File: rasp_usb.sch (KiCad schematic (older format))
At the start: 20 parts, among them J1 USB_B_Micro, J2 Conn_02x05_Odd_Even, U1 AMS1117-5.0, U2 FT230XQ

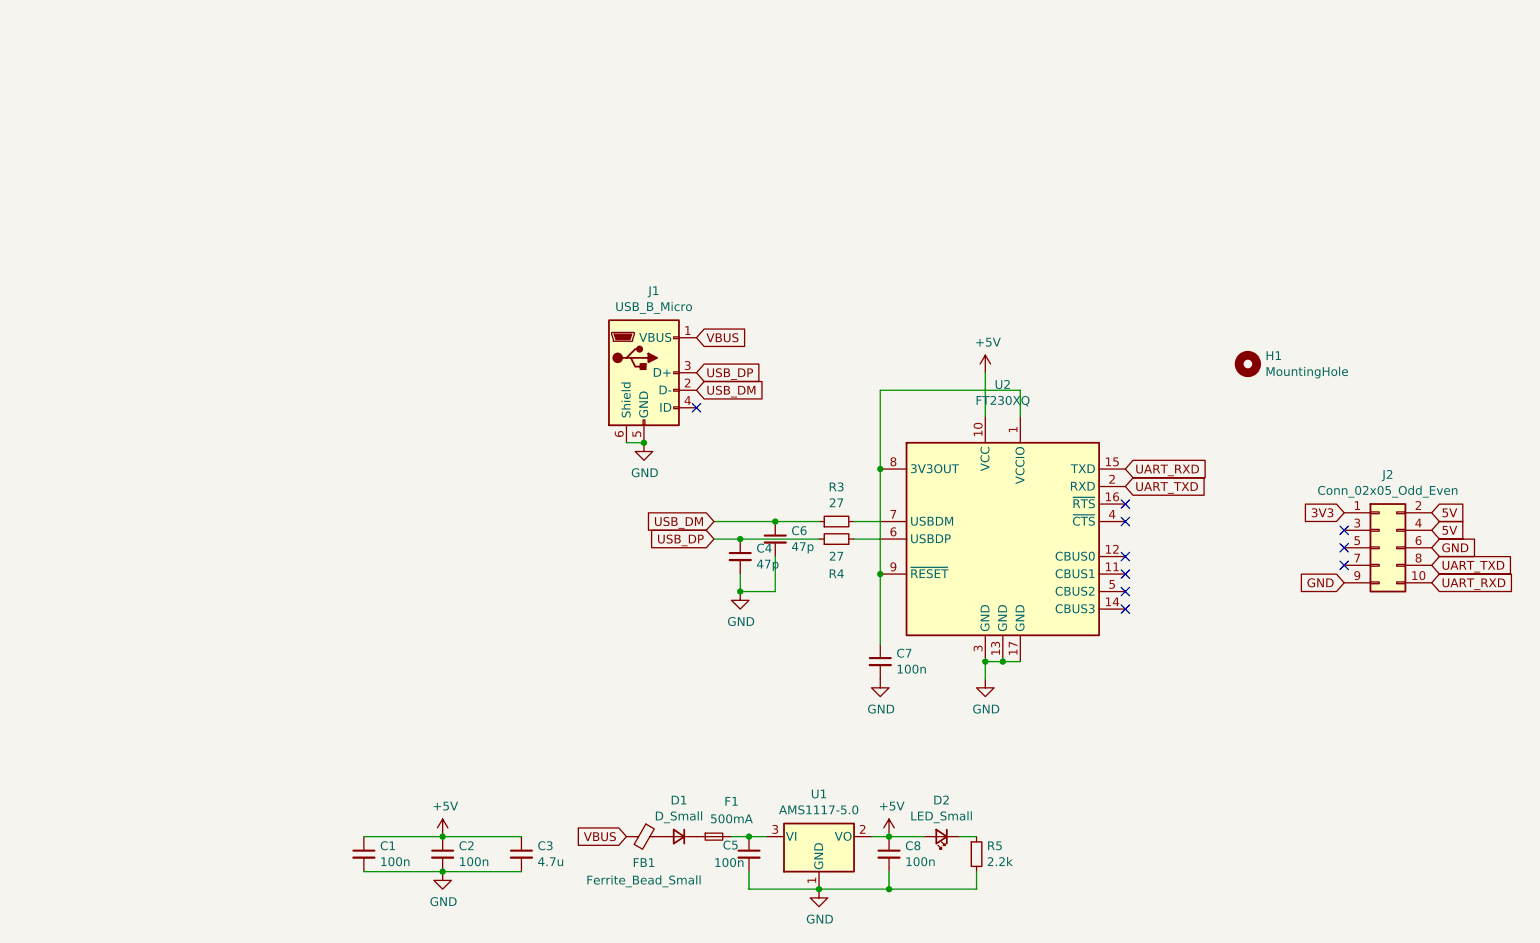
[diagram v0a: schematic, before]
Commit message: ftdi ic is out of stock
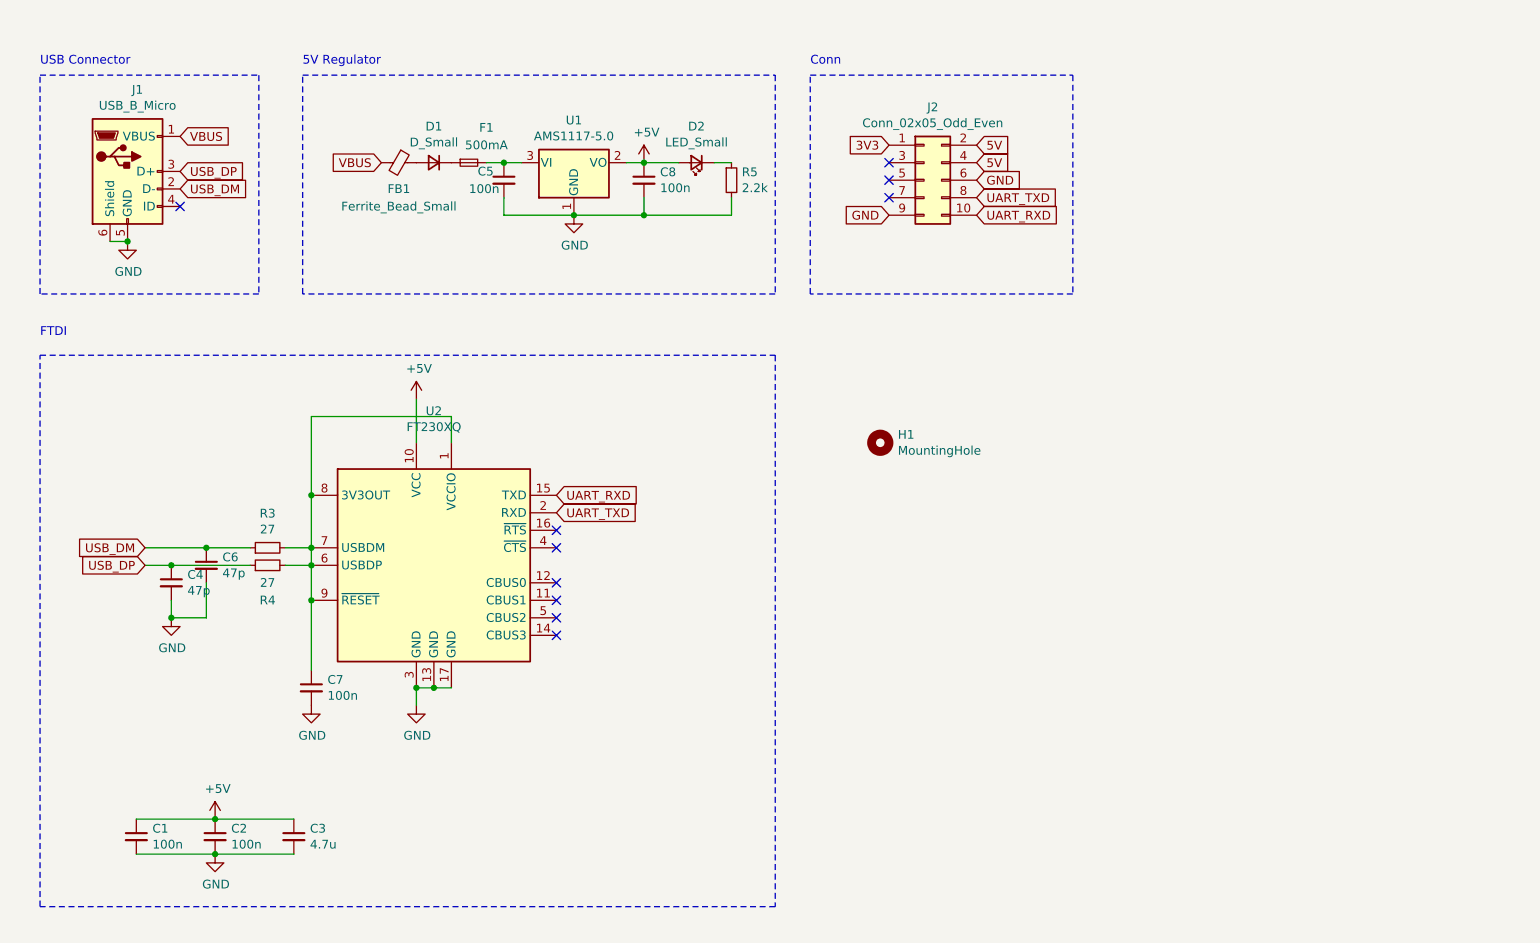
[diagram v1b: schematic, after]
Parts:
- D1: footprint Diode_SMD:D_0603_1608Metric -> Diode_SMD:D_SOD-123
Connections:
- net at C7.1, U2.1 (VCCIO), U2.8 (3V3OUT)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: now also R3.2, R4.2, U2.6 (USBDP), U2.7 (USBDM)
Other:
- note added: "5V Regulator"
- note added: "Conn"
- note added: "FTDI"
- note added: "USB Connector"
- moved on the sheet: C1, C2, C3, C4, C5, C6, C7, C8, D1, D2, F1, FB1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

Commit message: ready to order
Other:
- note added: "USB IC"
- note removed: "FTDI"
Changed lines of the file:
@@
 Wire Notes Line
 	1000 5850 1000 2700
-Text Notes 1000 2600 0    50   ~ 0
-FTDI
 Wire Notes Line
 	1000 1100 2250 1100
@@
 Text Notes 5400 1050 0    50   ~ 0
 Conn
+Text Notes 1050 2650 0    50   ~ 0
+USB IC
 $EndSCHEMATC

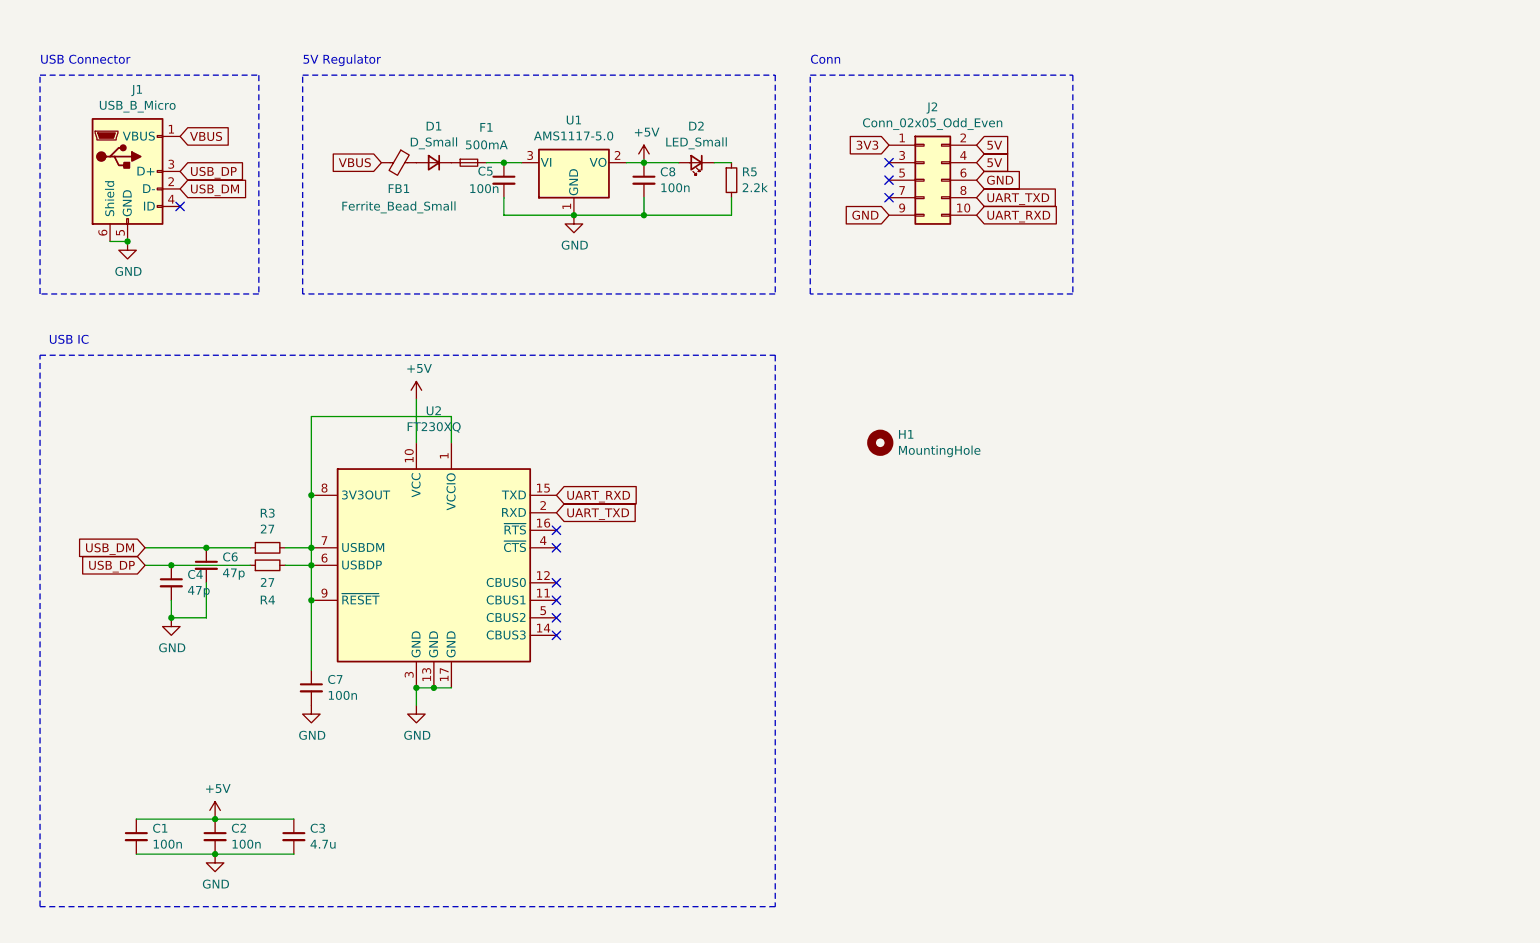
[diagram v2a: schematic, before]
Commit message: Replaced usb IC with cp2104. Ready to order
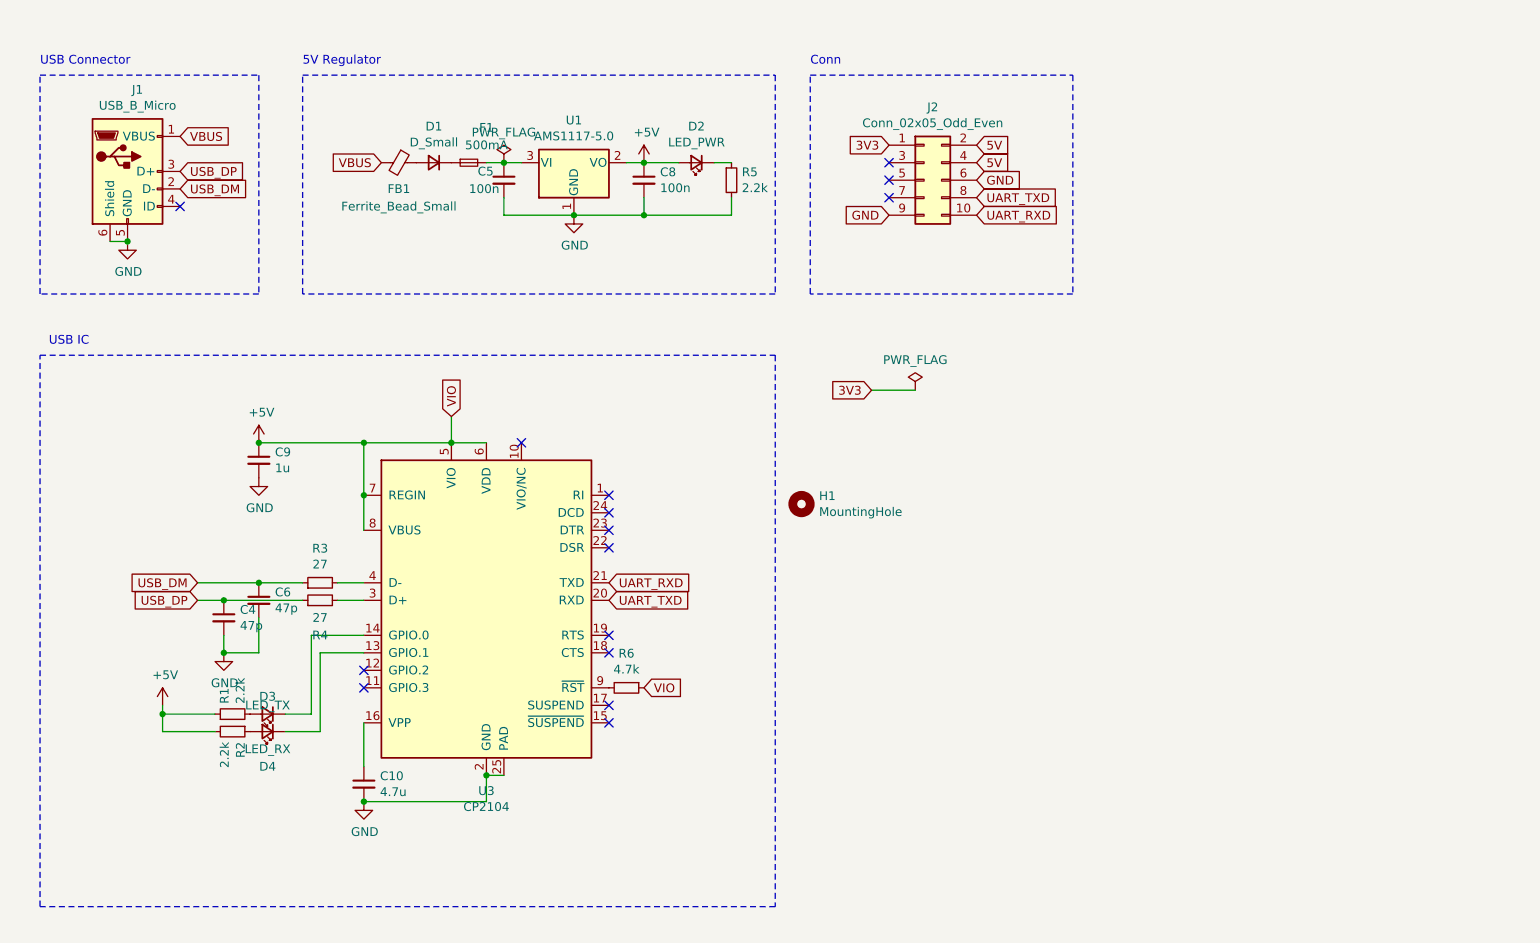
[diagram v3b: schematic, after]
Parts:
- removed C1, C2: 100n, Capacitor_SMD:C_0603_1608Metric, symbol Device:C_Small
- removed C3: 4.7u, Capacitor_SMD:C_0603_1608Metric, symbol Device:C_Small
- removed C7: 100n, Capacitor_SMD:C_0402_1005Metric, symbol Device:C_Small
- removed U2: FT230XQ, Package_DFN_QFN:QFN-16-1EP_4x4mm_P0.65mm_EP2.1x2.1mm, symbol Interface_USB:FT230XQ
- added C10: 4.7u, Capacitor_SMD:C_0603_1608Metric, symbol Device:C_Small
- added C9: 1u, Capacitor_SMD:C_0603_1608Metric, symbol Device:C_Small
- added D3: LED_TX, LED_SMD:LED_0402_1005Metric, symbol Device:LED_Small
- added D4: LED_RX, LED_SMD:LED_0402_1005Metric, symbol Device:LED_Small
- added R1, R2: 2.2k, Resistor_SMD:R_0402_1005Metric, symbol Device:R_Small
- added R6: 4.7k, Resistor_SMD:R_0402_1005Metric, symbol Device:R_Small
- added U3: CP2104, Package_DFN_QFN:QFN-24-1EP_4x4mm_P0.5mm_EP2.6x2.6mm, symbol Interface_USB:CP2104
- D2: value LED_Small -> LED_PWR; footprint LED_SMD:LED_0603_1608Metric -> LED_SMD:LED_0402_1005Metric
- R5: footprint Resistor_SMD:R_0603_1608Metric -> Resistor_SMD:R_0402_1005Metric
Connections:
- net +5V: now also C9.1, R1.1, R2.2, R6.1, U3.5 (VIO), U3.6 (VDD), U3.7 (REGIN), U3.8 (VBUS)
- net GND: now also C10.2, C9.2, U3.2 (GND), U3.25 (PAD)
- net UART_RXD: now also U3.21 (TXD)
- net UART_TXD: now also U3.20 (RXD)
- net at R3.2: now also U3.4 (D-); no longer R4.2
- new net: R4.2, U3.3 (D+)
- new net: D4.1 (K), U3.13 (GPIO.1)
- new net: D3.1 (K), U3.14 (GPIO.0)
- new net: C10.1, U3.16 (VPP)
- new net: R6.2, U3.9 (~RST)
- new net: D3.2 (A), R1.2
- new net: D4.2 (A), R2.1
- no-connect marks 10 -> 15
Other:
- moved on the sheet: C4, C6, H1, R3, R4

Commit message: ready to order
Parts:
- removed H1: MountingHole, MountingHole:MountingHole_2.7mm_M2.5, symbol Mechanical:MountingHole
- J1: footprint Connector_USB:USB_Micro-B_Amphenol_10103594-0001LF_Horizontal -> Connector_USB:USB_Micro-B_Amphenol_10104110_Horizontal
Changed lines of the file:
@@
 Date "2020-11-23"
 Rev ""
-Comp "BitEngineers"
+Comp ""
 Comment1 ""
 Comment2 ""
@@
 Connection ~ 4450 1900
 $Comp
-L Mechanical:MountingHole H1
-U 1 1 5FCD5980
-P 5350 3550
-F 0 "H1" H 5450 3596 50  0000 L CNN
-F 1 "MountingHole" H 5450 3505 50  0000 L CNN
-F 2 "MountingHole:MountingHole_2.7mm_M2.5" H 5350 3550 50  0001 C CNN
-F 3 "~" H 5350 3550 50  0001 C CNN
-	1    5350 3550
-	1    0    0    -1
-$EndComp
-$Comp
 L Connector:USB_B_Micro J1
 U 1 1 5FD1A450
@@
 F 0 "J1" H 1557 2117 50  0000 C CNN
 F 1 "USB_B_Micro" H 1557 2026 50  0000 C CNN
-F 2 "Connector_USB:USB_Micro-B_Amphenol_10103594-0001LF_Horizontal" H 1650 1600 50  0001 C CNN
+F 2 "Connector_USB:USB_Micro-B_Amphenol_10104110_Horizontal" H 1650 1600 50  0001 C CNN
 F 3 "~" H 1650 1600 50  0001 C CNN
 	1    1500 1650

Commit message: Updated schematics as hierarchical structure
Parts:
- removed C10: 4.7u, Capacitor_SMD:C_0603_1608Metric, symbol Device:C_Small
- removed C4, C6: 47p, Capacitor_SMD:C_0402_1005Metric, symbol Device:C_Small
- removed C5, C8: 100n, Capacitor_SMD:C_0603_1608Metric, symbol Device:C_Small
- removed C9: 1u, Capacitor_SMD:C_0603_1608Metric, symbol Device:C_Small
- removed D1: D_Small, Diode_SMD:D_SOD-123, symbol Device:D_Small
- removed D2: LED_PWR, LED_SMD:LED_0402_1005Metric, symbol Device:LED_Small
- removed D3: LED_TX, LED_SMD:LED_0402_1005Metric, symbol Device:LED_Small
- removed D4: LED_RX, LED_SMD:LED_0402_1005Metric, symbol Device:LED_Small
- removed F1: 500mA, Fuse:Fuse_0603_1608Metric, symbol Device:Fuse_Small
- removed FB1: Ferrite_Bead_Small, Inductor_SMD:L_0603_1608Metric, symbol Device:Ferrite_Bead_Small
- removed J1: USB_B_Micro, Connector_USB:USB_Micro-B_Amphenol_10104110_Horizontal, symbol Connector:USB_B_Micro
- removed R1, R2, R5: 2.2k, Resistor_SMD:R_0402_1005Metric, symbol Device:R_Small
- removed R3, R4: 27, Resistor_SMD:R_0402_1005Metric, symbol Device:R_Small
- removed R6: 4.7k, Resistor_SMD:R_0402_1005Metric, symbol Device:R_Small
- removed U1: AMS1117-5.0, Package_TO_SOT_SMD:SOT-223-3_TabPin2, symbol Regulator_Linear:AMS1117-5.0
- removed U3: CP2104, Package_DFN_QFN:QFN-24-1EP_4x4mm_P0.5mm_EP2.6x2.6mm, symbol Interface_USB:CP2104
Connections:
- no-connect marks 15 -> 3
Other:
- note removed: "5V Regulator"
- note removed: "USB Connector"
- note removed: "USB IC"

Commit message: annotation number
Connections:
- net 3V3 renamed +3V3
- net 5V renamed +5V
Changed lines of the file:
@@
 	1    0    0    -1
 $EndComp
-Text GLabel 6350 1500 2    50   Input ~ 0
-5V
-Text GLabel 6350 1700 2    50   Input ~ 0
-GND
 Text GLabel 6350 1800 2    50   Input ~ 0
 UART_TXD
 Text GLabel 6350 1900 2    50   Input ~ 0
 UART_RXD
-Text GLabel 5850 1900 0    50   Input ~ 0
-GND
-Text GLabel 5850 1500 0    50   Input ~ 0
-3V3
-Text GLabel 6350 1600 2    50   Input ~ 0
-5V
 NoConn ~ 5850 1600
 NoConn ~ 5850 1700
@@
 Text Notes 5400 1050 0    50   ~ 0
 Conn
-Text GLabel 5750 2900 0    50   Input ~ 0
-3V3
-$Comp
-L power:PWR_FLAG #FLG0102
-U 1 1 5FD5B3BE
-P 6000 2900
-F 0 "#FLG0102" H 6000 2975 50  0001 C CNN
-F 1 "PWR_FLAG" H 6000 3073 50  0000 C CNN
-F 2 "" H 6000 2900 50  0001 C CNN
-F 3 "~" H 6000 2900 50  0001 C CNN
-	1    6000 2900
-	1    0    0    -1
-$EndComp
-Wire Wire Line
-	5750 2900 6000 2900
 $Sheet
 S 2150 900  1050 500
@@
 F1 "usb_ic.sch" 50
 $EndSheet
+$Comp
+L power:+5V #PWR0110
+U 1 1 5FFC6082
+P 6600 1500
+F 0 "#PWR0110" H 6600 1350 50  0001 C CNN
+F 1 "+5V" H 6615 1673 50  0000 C CNN
+F 2 "" H 6600 1500 50  0001 C CNN
+F 3 "" H 6600 1500 50  0001 C CNN
+	1    6600 1500
+	1    0    0    -1
+$EndComp
+Wire Wire Line
+	6350 1500 6600 1500
+Wire Wire Line
+	6350 1600 6600 1600
+Wire Wire Line
+	6600 1600 6600 1500
+Connection ~ 6600 1500
+$Comp
+L power:+3.3V #PWR0111
+U 1 1 5FFC6F8E
+P 5550 1500
+F 0 "#PWR0111" H 5550 1350 50  0001 C CNN
+F 1 "+3.3V" H 5565 1673 50  0000 C CNN
+F 2 "" H 5550 1500 50  0001 C CNN
+F 3 "" H 5550 1500 50  0001 C CNN
+	1    5550 1500
+	1    0    0    -1
+$EndComp
+Wire Wire Line
+	5550 1500 5850 1500
+$Comp
+L power:GND #PWR0112
+U 1 1 5FFC7D97
+P 5550 1900
+F 0 "#PWR0112" H 5550 1650 50  0001 C CNN
+F 1 "GND" H 5555 1727 50  0000 C CNN
+F 2 "" H 5550 1900 50  0001 C CNN
+F 3 "" H 5550 1900 50  0001 C CNN
+	1    5550 1900
+	1    0    0    -1
+$EndComp
+Wire Wire Line
+	5850 1900 5550 1900
+$Comp
+L power:GND #PWR0113
+U 1 1 5FFC88A9
+P 6650 2050
+F 0 "#PWR0113" H 6650 1800 50  0001 C CNN
+F 1 "GND" H 6655 1877 50  0000 C CNN
+F 2 "" H 6650 2050 50  0001 C CNN
+F 3 "" H 6650 2050 50  0001 C CNN
+	1    6650 2050
+	1    0    0    -1
+$EndComp
+Wire Wire Line
+	6350 1700 6850 1700
+Wire Wire Line
+	6850 1700 6850 2050
+Wire Wire Line
+	6850 2050 6650 2050
 $EndSCHEMATC

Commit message: Ready to order
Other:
- moved on the sheet: J2
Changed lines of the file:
@@
 L Connector_Generic:Conn_02x05_Odd_Even J2
 U 1 1 5FBEC2E7
-P 6050 1700
-F 0 "J2" H 6100 2117 50  0000 C CNN
-F 1 "Conn_02x05_Odd_Even" H 6100 2026 50  0000 C CNN
-F 2 "Connector_PinSocket_2.54mm:PinSocket_2x05_P2.54mm_Vertical" H 6050 1700 50  0001 C CNN
-F 3 "~" H 6050 1700 50  0001 C CNN
-	1    6050 1700
+P 1500 4000
+F 0 "J2" H 1550 4417 50  0000 C CNN
+F 1 "Conn_02x05_Odd_Even" H 1550 4326 50  0000 C CNN
+F 2 "Connector_PinSocket_2.54mm:PinSocket_2x05_P2.54mm_Vertical" H 1500 4000 50  0001 C CNN
+F 3 "~" H 1500 4000 50  0001 C CNN
+	1    1500 4000
 	1    0    0    -1
 $EndComp
-Text GLabel 6350 1800 2    50   Input ~ 0
+Text GLabel 1800 4100 2    50   Input ~ 0
 UART_TXD
-Text GLabel 6350 1900 2    50   Input ~ 0
+Text GLabel 1800 4200 2    50   Input ~ 0
 UART_RXD
-NoConn ~ 5850 1600
-NoConn ~ 5850 1700
-NoConn ~ 5850 1800
+NoConn ~ 1300 3900
+NoConn ~ 1300 4000
+NoConn ~ 1300 4100
 Wire Notes Line
-	5400 1100 6900 1100
+	850  3400 2350 3400
 Wire Notes Line
-	6900 1100 6900 2350
+	2350 3400 2350 4650
 Wire Notes Line
-	6900 2350 5400 2350
+	2350 4650 850  4650
 Wire Notes Line
-	5400 2350 5400 1100
-Text Notes 5400 1050 0    50   ~ 0
+	850  4650 850  3400
+Text Notes 850  3350 0    50   ~ 0
 Conn
 $Sheet
@@
 L power:+5V #PWR0110
 U 1 1 5FFC6082
-P 6600 1500
-F 0 "#PWR0110" H 6600 1350 50  0001 C CNN
-F 1 "+5V" H 6615 1673 50  0000 C CNN
-F 2 "" H 6600 1500 50  0001 C CNN
-F 3 "" H 6600 1500 50  0001 C CNN
-	1    6600 1500
+P 2050 3800
+F 0 "#PWR0110" H 2050 3650 50  0001 C CNN
+F 1 "+5V" H 2065 3973 50  0000 C CNN
+F 2 "" H 2050 3800 50  0001 C CNN
+F 3 "" H 2050 3800 50  0001 C CNN
+	1    2050 3800
 	1    0    0    -1
 $EndComp
 Wire Wire Line
-	6350 1500 6600 1500
+	1800 3800 2050 3800
 Wire Wire Line
-	6350 1600 6600 1600
+	1800 3900 2050 3900
 Wire Wire Line
-	6600 1600 6600 1500
-Connection ~ 6600 1500
+	2050 3900 2050 3800
+Connection ~ 2050 3800
 $Comp
 L power:+3.3V #PWR0111
 U 1 1 5FFC6F8E
-P 5550 1500
-F 0 "#PWR0111" H 5550 1350 50  0001 C CNN
-F 1 "+3.3V" H 5565 1673 50  0000 C CNN
-F 2 "" H 5550 1500 50  0001 C CNN
-F 3 "" H 5550 1500 50  0001 C CNN
-	1    5550 1500
+P 1000 3800
+F 0 "#PWR0111" H 1000 3650 50  0001 C CNN
+F 1 "+3.3V" H 1015 3973 50  0000 C CNN
+F 2 "" H 1000 3800 50  0001 C CNN
+F 3 "" H 1000 3800 50  0001 C CNN
+	1    1000 3800
 	1    0    0    -1
 $EndComp
 Wire Wire Line
-	5550 1500 5850 1500
+	1000 3800 1300 3800
 $Comp
 L power:GND #PWR0112
 U 1 1 5FFC7D97
-P 5550 1900
-F 0 "#PWR0112" H 5550 1650 50  0001 C CNN
-F 1 "GND" H 5555 1727 50  0000 C CNN
-F 2 "" H 5550 1900 50  0001 C CNN
-F 3 "" H 5550 1900 50  0001 C CNN
-	1    5550 1900
+P 1000 4200
+F 0 "#PWR0112" H 1000 3950 50  0001 C CNN
+F 1 "GND" H 1005 4027 50  0000 C CNN
+F 2 "" H 1000 4200 50  0001 C CNN
+F 3 "" H 1000 4200 50  0001 C CNN
+	1    1000 4200
 	1    0    0    -1
 $EndComp
 Wire Wire Line
-	5850 1900 5550 1900
+	1300 4200 1000 4200
 $Comp
 L power:GND #PWR0113
 U 1 1 5FFC88A9
-P 6650 2050
-F 0 "#PWR0113" H 6650 1800 50  0001 C CNN
-F 1 "GND" H 6655 1877 50  0000 C CNN
-F 2 "" H 6650 2050 50  0001 C CNN
-F 3 "" H 6650 2050 50  0001 C CNN
-	1    6650 2050
+P 2100 4350
+F 0 "#PWR0113" H 2100 4100 50  0001 C CNN
+F 1 "GND" H 2105 4177 50  0000 C CNN
+F 2 "" H 2100 4350 50  0001 C CNN
+F 3 "" H 2100 4350 50  0001 C CNN
+	1    2100 4350
 	1    0    0    -1
 $EndComp
 Wire Wire Line
-	6350 1700 6850 1700
+	1800 4000 2300 4000
 Wire Wire Line
-	6850 1700 6850 2050
+	2300 4000 2300 4350
 Wire Wire Line
-	6850 2050 6650 2050
+	2300 4350 2100 4350
 $EndSCHEMATC
